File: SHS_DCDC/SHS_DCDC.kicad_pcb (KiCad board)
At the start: 4 copper layers, 100 x 100 mm, 104 parts, among them J1 Barrel_Jack, J2 USB_A, Q1 BSS84, Q10 PMV100XPEAR, Q11 PMV100XPEAR, Q12 PMV100XPEAR, Q13 PMV100XPEAR, Q2 PMV100XPEAR, Q3 2N7002, Q4 2N7002, Q5 PMV100XPEAR, Q6 2N7002, Q7 PMV100XPEAR, Q8 Q_PMOS_DGS, Q9 PMV100XPEAR, U1 A0Z1283, U2 INA181, U3 LMV324AIDR, U4 LMV358IDR, U5 MP3414A, U6 STM32G050K8T6, U7 MCP101

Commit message: 20213110
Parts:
- added U8: RT8299-WDFN10L, SHS_DCDC:RT8299-WDFN, F.Cu at (17.2, 67.2)
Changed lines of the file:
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@@
     (tracks 313)
     (zones 0)
-    (modules 104)
-    (nets 102)
+    (modules 105)
+    (nets 110)
   )
   (page A4)
@@
   )
   (setup
-    (last_trace_width 0.5)
+    (last_trace_width 0.25)
     (user_trace_width 0.4)
     (user_trace_width 0.5)
@@
   (net 100 MCU_TX)
   (net 101 "Net-(Q13-Pad1)")
+  (net 102 "Net-(U8-Pad1)")
+  (net 103 "Net-(U8-Pad2)")
+  (net 104 "Net-(U8-Pad3)")
+  (net 105 "Net-(U8-Pad4)")
+  (net 106 "Net-(U8-Pad7)")
+  (net 107 "Net-(U8-Pad6)")
+  (net 108 "Net-(U8-Pad8)")
+  (net 109 "Net-(U8-Pad10)")
   (net_class Default "This is the default net class."
     (clearance 0.2)
@@
     (add_net "Net-(U6-Pad8)")
     (add_net "Net-(U6-Pad9)")
+    (add_net "Net-(U8-Pad1)")
+    (add_net "Net-(U8-Pad10)")
+    (add_net "Net-(U8-Pad2)")
+    (add_net "Net-(U8-Pad3)")
+    (add_net "Net-(U8-Pad4)")
+    (add_net "Net-(U8-Pad6)")
+    (add_net "Net-(U8-Pad7)")
+    (add_net "Net-(U8-Pad8)")
     (add_net OP_CUR_BL1+)
     (add_net OP_CUR_BL1-)
@@
     (add_net V_MCU)
   )
+  (module SHS_DCDC:RT8299-WDFN (layer F.Cu)
+    (at 17.2 67.2)
+    (fp_text reference U8 (at 0.84 -2.337) (layer F.SilkS)
+      (effects (font (size 1 1) (thickness 0.15)))
+    )
+    (fp_text value RT8299-WDFN10L (at 10.365 2.337) (layer F.Fab)
+      (effects (font (size 1 1) (thickness 0.15)))
+    )
+    (fp_circle (center -2.636 -1.133) (end -2.486 -1.133) (layer F.SilkS) (width 0.2))
+    (fp_circle (center -2.636 -1.133) (end -2.486 -1.133) (layer F.Fab) (width 0.2))
+    (fp_line (start -1.53 -1.53) (end 1.53 -1.53) (layer F.Fab) (width 0.127))
+    (fp_line (start -1.53 1.53) (end 1.53 1.53) (layer F.Fab) (width 0.127))
+    (fp_line (start -1.53 -1.551) (end 1.53 -1.551) (layer F.SilkS) (width 0.127))
+    (fp_line (start -1.53 1.551) (end 1.53 1.551) (layer F.SilkS) (width 0.127))
+    (fp_line (start -1.53 -1.53) (end -1.53 1.53) (layer F.Fab) (width 0.127))
+    (fp_line (start 1.53 -1.53) (end 1.53 1.53) (layer F.Fab) (width 0.127))
+    (fp_line (start -2.1 -1.78) (end 2.1 -1.78) (layer F.CrtYd) (width 0.05))
+    (fp_line (start -2.1 1.78) (end 2.1 1.78) (layer F.CrtYd) (width 0.05))
+    (fp_line (start -2.1 -1.78) (end -2.1 1.78) (layer F.CrtYd) (width 0.05))
+    (fp_line (start 2.1 -1.78) (end 2.1 1.78) (layer F.CrtYd) (width 0.05))
+    (fp_poly (pts (xy -0.625 -1.045) (xy -0.095 -1.045) (xy -0.095 -0.095) (xy -0.625 -0.095)) (layer F.Paste) (width 0.01))
+    (fp_poly (pts (xy -0.625 0.095) (xy -0.095 0.095) (xy -0.095 1.045) (xy -0.625 1.045)) (layer F.Paste) (width 0.01))
+    (fp_poly (pts (xy 0.095 -1.045) (xy 0.625 -1.045) (xy 0.625 -0.095) (xy 0.095 -0.095)) (layer F.Paste) (width 0.01))
+    (fp_poly (pts (xy 0.095 0.095) (xy 0.625 0.095) (xy 0.625 1.045) (xy 0.095 1.045)) (layer F.Paste) (width 0.01))
+    (pad 1 smd roundrect (at -1.475 -1) (size 0.85 0.3) (layers F.Cu F.Paste F.Mask) (roundrect_rratio 0.03)
+      (net 102 "Net-(U8-Pad1)"))
+    (pad 2 smd roundrect (at -1.475 -0.5) (size 0.85 0.3) (layers F.Cu F.Paste F.Mask) (roundrect_rratio 0.03)
+      (net 103 "Net-(U8-Pad2)"))
+    (pad 3 smd roundrect (at -1.475 0) (size 0.85 0.3) (layers F.Cu F.Paste F.Mask) (roundrect_rratio 0.03)
+      (net 104 "Net-(U8-Pad3)"))
+    (pad 4 smd roundrect (at -1.475 0.5) (size 0.85 0.3) (layers F.Cu F.Paste F.Mask) (roundrect_rratio 0.03)
+      (net 105 "Net-(U8-Pad4)"))
+    (pad 5 smd roundrect (at -1.475 1) (size 0.85 0.3) (layers F.Cu F.Paste F.Mask) (roundrect_rratio 0.03))
+    (pad 6 smd roundrect (at 1.475 1) (size 0.85 0.3) (layers F.Cu F.Paste F.Mask) (roundrect_rratio 0.03)
+      (net 107 "Net-(U8-Pad6)"))
+    (pad 7 smd roundrect (at 1.475 0.5) (size 0.85 0.3) (layers F.Cu F.Paste F.Mask) (roundrect_rratio 0.03)
+      (net 106 "Net-(U8-Pad7)"))
+    (pad 8 smd roundrect (at 1.475 0) (size 0.85 0.3) (layers F.Cu F.Paste F.Mask) (roundrect_rratio 0.03)
+      (net 108 "Net-(U8-Pad8)"))
+    (pad 9 smd roundrect (at 1.475 -0.5) (size 0.85 0.3) (layers F.Cu F.Paste F.Mask) (roundrect_rratio 0.03))
+    (pad 10 smd roundrect (at 1.475 -1) (size 0.85 0.3) (layers F.Cu F.Paste F.Mask) (roundrect_rratio 0.03)
+      (net 109 "Net-(U8-Pad10)"))
+    (pad 11 smd rect (at 0 0) (size 1.7 2.55) (layers F.Cu F.Mask))
+  )
   (module Capacitor_SMD:C_0402_1005Metric (layer F.Cu)
     (at 76.4 70.5 270)
@@
     (fp_text value 100nF (at 0 1.16 90) (layer F.Fab)
       (effects (font (size 1 1) (thickness 0.15)))
-    )
-    (fp_text user %R (at 0 0 90) (layer F.Fab)
-      (effects (font (size 0.25 0.25) (thickness 0.04)))
     )
     (fp_line (start -0.5 0.25) (end -0.5 -0.25) (layer F.Fab) (width 0.1))
@@
     (fp_line (start 0.91 -0.46) (end 0.91 0.46) (layer F.CrtYd) (width 0.05))
     (fp_line (start 0.91 0.46) (end -0.91 0.46) (layer F.CrtYd) (width 0.05))
+    (fp_text user %R (at 0 0 90) (layer F.Fab)
+      (effects (font (size 0.25 0.25) (thickness 0.04)))
+    )
     (pad 2 smd roundrect (at 0.48 0 270) (size 0.56 0.62) (layers F.Cu F.Paste F.Mask) (roundrect_rratio 0.25)
       (net 15 V_MCU))
@@
     (fp_text value PMV100XPEAR (at 0.025 3.25) (layer F.Fab)
       (effects (font (size 1 1) (thickness 0.15)))
-    )
-    (fp_text user %R (at -0.125 0.15) (layer F.Fab)
-      (effects (font (size 0.25 0.25) (thickness 0.05)))
     )
     (fp_line (start -1.825 -1.95) (end 1.825 -1.95) (layer F.CrtYd) (width 0.05))
@@
     (fp_line (start -0.7 1.52) (end 0.7 1.52) (layer F.Fab) (width 0.1))
     (fp_line (start 0.7 1.52) (end 0.7 -1.52) (layer F.Fab) (width 0.1))
+    (fp_text user %R (at -0.125 0.15) (layer F.Fab)
+      (effects (font (size 0.25 0.25) (thickness 0.05)))
+    )
     (pad 1 smd rect (at -1.05 -0.95) (size 1.3 0.6) (layers F.Cu F.Paste F.Mask)
       (net 101 "Net-(Q13-Pad1)") (solder_mask_margin 0.07))
@@
     (fp_text value 4.7uF (at 0 1.43 90) (layer F.Fab)
       (effects (font (size 1 1) (thickness 0.15)))
-    )
-    (fp_text user %R (at 0 0 90) (layer F.Fab)
-      (effects (font (size 0.4 0.4) (thickness 0.06)))
     )
     (fp_line (start -0.8 0.4) (end -0.8 -0.4) (layer F.Fab) (width 0.1))
@@
     (fp_line (start 1.48 -0.73) (end 1.48 0.73) (layer F.CrtYd) (width 0.05))
     (fp_line (start 1.48 0.73) (end -1.48 0.73) (layer F.CrtYd) (width 0.05))
+    (fp_text user %R (at 0 0 90) (layer F.Fab)
+      (effects (font (size 0.4 0.4) (thickness 0.06)))
+    )
     (pad 2 smd roundrect (at 0.775 0 270) (size 0.9 0.95) (layers F.Cu F.Paste F.Mask) (roundrect_rratio 0.25)
       (net 15 V_MCU))
@@
     (fp_text value 10uF (at 0 1.43 90) (layer F.Fab)
       (effects (font (size 1 1) (thickness 0.15)))
-    )
-    (fp_text user %R (at 0 0 90) (layer F.Fab)
-      (effects (font (size 0.4 0.4) (thickness 0.06)))
     )
     (fp_line (start -0.8 0.4) (end -0.8 -0.4) (layer F.Fab) (width 0.1))
@@
     (fp_line (start 1.48 -0.73) (end 1.48 0.73) (layer F.CrtYd) (width 0.05))
     (fp_line (start 1.48 0.73) (end -1.48 0.73) (layer F.CrtYd) (width 0.05))
+    (fp_text user %R (at 0 0 90) (layer F.Fab)
+      (effects (font (size 0.4 0.4) (thickness 0.06)))
+    )
     (pad 2 smd roundrect (at 0.775 0 270) (size 0.9 0.95) (layers F.Cu F.Paste F.Mask) (roundrect_rratio 0.25)
       (net 13 DCDC_OUT))
@@
     (fp_text value 100nF (at 0 1.43) (layer F.Fab)
       (effects (font (size 1 1) (thickness 0.15)))
-    )
-    (fp_text user %R (at 0 0) (layer F.Fab)
-      (effects (font (size 0.4 0.4) (thickness 0.06)))
     )
     (fp_line (start -0.8 0.4) (end -0.8 -0.4) (layer F.Fab) (width 0.1))
@@
     (fp_line (start 1.48 -0.73) (end 1.48 0.73) (layer F.CrtYd) (width 0.05))
     (fp_line (start 1.48 0.73) (end -1.48 0.73) (layer F.CrtYd) (width 0.05))
+    (fp_text user %R (at 0 0) (layer F.Fab)
+      (effects (font (size 0.4 0.4) (thickness 0.06)))
+    )
     (pad 2 smd roundrect (at 0.775 0) (size 0.9 0.95) (layers F.Cu F.Paste F.Mask) (roundrect_rratio 0.25)
       (net 4 GND))

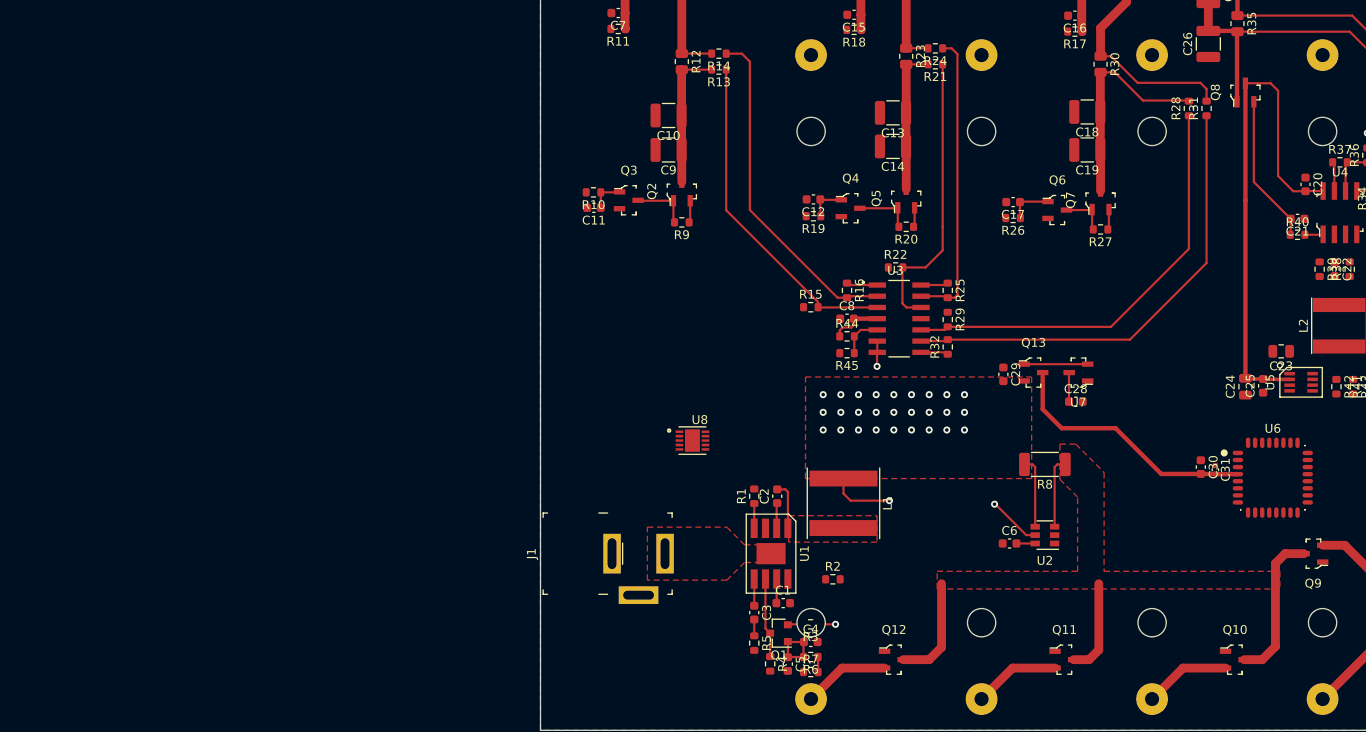
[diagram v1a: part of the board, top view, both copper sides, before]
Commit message: esp32 s2 mini placed
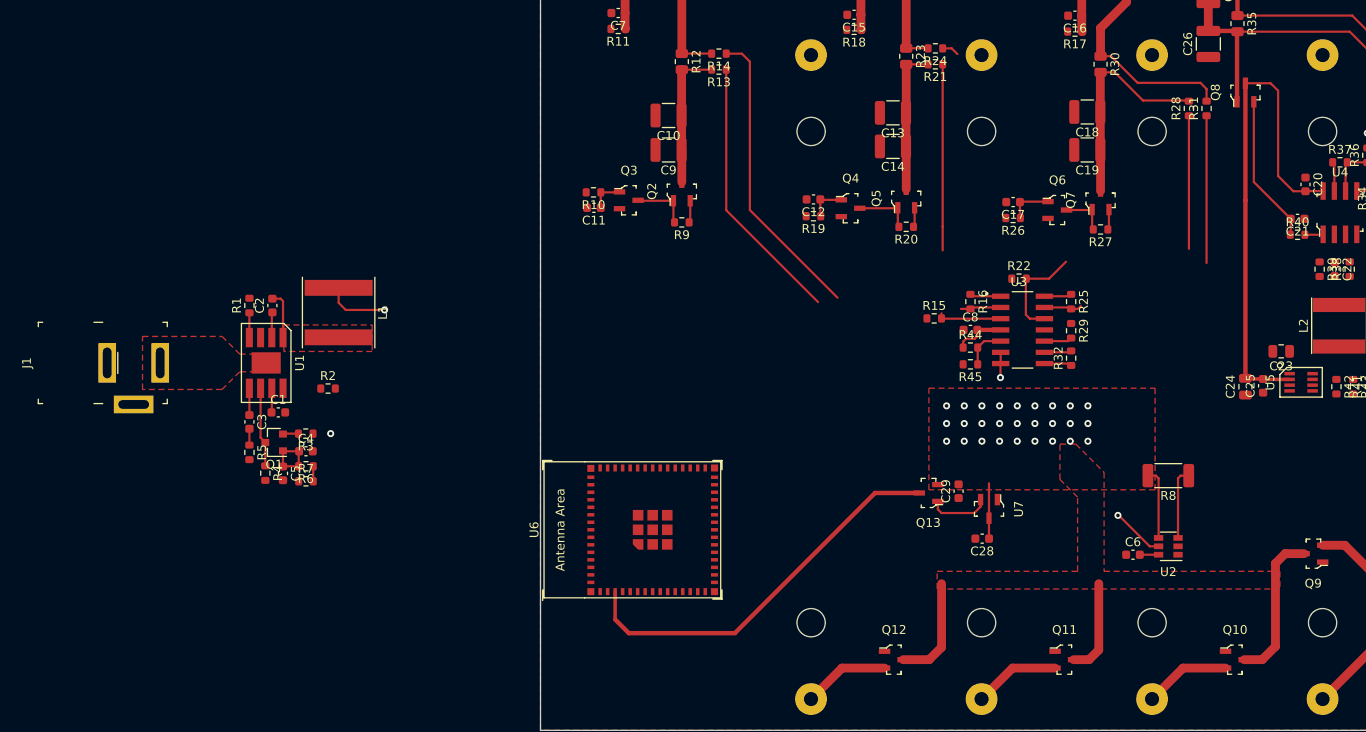
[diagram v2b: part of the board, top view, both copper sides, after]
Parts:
- removed C30: 4.7uF, Capacitor_SMD:C_0603_1608Metric
- removed C31: 100nF, Capacitor_SMD:C_0402_1005Metric
- removed U8: RT8299-WDFN10L, SHS_DCDC:RT8299-WDFN
- 4cells1: footprint SHS_DCDC:BK-18650-PC8 -> BK-18650:BK-18650-PC8
- U6: value STM32G050K8T6 -> ESP32-S2-MINI-1; footprint SHS_DCDC:STM320G50_LQFP32 -> Espressif:ESP32-S2-MINI-1
- moved U6 70.4 mm to (12.7, 77.3), turned to 90 degrees
- moved C2 61.1 mm to (-30.4, 51.9)
- moved C3 61.1 mm to (-33.0, 65.1)
- moved C4 61.1 mm to (-26.6, 68.4)
- moved R1 61.1 mm to (-33.0, 51.9)
- moved R2 61.1 mm to (-24.1, 61.3)
- moved R5 61.1 mm to (-33.0, 68.5)
- moved R6 61.1 mm to (-26.6, 70.1)
- moved R7 61.1 mm to (-26.6, 71.8)
- moved U1 61.1 mm to (-31.1, 58.4)
- moved C1 61.1 mm to (-29.7, 64.0)
- moved C5 61.1 mm to (-29.1, 70.9)
- moved J1 61.1 mm to (-46.0, 58.4)
- moved L1 61.1 mm to (-22.9, 52.7)
- moved Q1 61.1 mm to (-30.1, 67.4)
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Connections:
- Bulb1 pad 1: Net-(Bulb1-Pad1) -> (no net)
- Bulb2 pad 1: Net-(Bulb2-Pad1) -> (no net)
- R10 pad 2: MCU_PWM_TL -> (no net)
- R19 pad 2: MCU_PWM_BL1 -> (no net)
- R2 pad 2: Net-(R2-Pad2) -> (no net)
- R26 pad 2: MCU_PWM_BL2 -> (no net)
- R39 pad 2: ILIM_USB -> (no net)
- R41 pad 1: MCU_5V_EN -> (no net)
- TubeLight1 pad 2: Net-(TubeLight1-Pad2) -> (no net)
- U2 pad 1: MCU_ADC_BAT -> (no net)
- U6 pad 1: Net-(U6-Pad1) -> GND
- U6 pad 10: Net-(U6-Pad10) -> (no net)
- U6 pad 11: Net-(U6-Pad11) -> (no net)
- U6 pad 12: Net-(U6-Pad12) -> (no net)
- U6 pad 13: Net-(U6-Pad13) -> (no net)
- U6 pad 14: Net-(U6-Pad14) -> (no net)
- U6 pad 15: Net-(U6-Pad15) -> (no net)
- U6 pad 16: Net-(U6-Pad16) -> (no net)
- U6 pad 17: Net-(U6-Pad17) -> (no net)
- U6 pad 18: Net-(U6-Pad18) -> (no net)
- U6 pad 19: Net-(U6-Pad19) -> (no net)
- U6 pad 2: Net-(U6-Pad2) -> GND
- U6 pad 20: Net-(U6-Pad20) -> (no net)
- U6 pad 21: Net-(U6-Pad21) -> (no net)
- U6 pad 22: Net-(U6-Pad22) -> (no net)
- U6 pad 23: Net-(U6-Pad23) -> (no net)
- U6 pad 24: Net-(U6-Pad24) -> (no net)
- U6 pad 25: Net-(U6-Pad25) -> (no net)
- U6 pad 26: Net-(U6-Pad26) -> (no net)
- U6 pad 27: Net-(U6-Pad27) -> (no net)
- U6 pad 28: Net-(U6-Pad28) -> (no net)
- U6 pad 29: Net-(U6-Pad29) -> (no net)
- U6 pad 3: Net-(U6-Pad3) -> V_MCU
- U6 pad 30: MCU_TX -> GND
- U6 pad 31: MCU_RX -> (no net)
- U6 pad 32: Net-(U6-Pad32) -> (no net)
- U6 pad 4: V_MCU -> (no net)
- U6 pad 5: Net-(U6-Pad5) -> (no net)
- U6 pad 6: Net-(U6-Pad6) -> (no net)
- U6 pad 7: Net-(U6-Pad7) -> (no net)
- U6 pad 8: Net-(U6-Pad8) -> (no net)
- U6 pad 9: Net-(U6-Pad9) -> (no net)
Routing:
- net OP_CUR_BL2-: track 52.7 -> 19.8 mm
- net OP_CUR_BL2+: track 49.2 -> 18.2 mm
- net OP_CUR_BL1-: track 33.5 -> 6.27 mm
- net V_MCU: track 37.3 -> 52.8 mm
- net DCDC_OUT: track 45.3 -> 46.3 mm

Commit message: Commit_GitHubgDesktop
Try of Github desktop
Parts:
- removed C28: 100nF, Capacitor_SMD:C_0603_1608Metric
- removed R21, R24, R28, R31: 1k1%, Resistor_SMD:R_0603_1608Metric
- removed R22, R25, R29, R32: 20k1%, Resistor_SMD:R_0603_1608Metric
- removed R23, R30: 150mOhm, Resistor_SMD:R_0805_2012Metric
- removed R44, R45: 100k+, Resistor_SMD:R_0603_1608Metric
- added C30: 10 uF, Capacitor_SMD:C_0805_2012Metric, F.Cu at (22.0, 45.1)
- added C31: 10 uF, Capacitor_SMD:C_0805_2012Metric, F.Cu at (20.0, 45.1)
- added C32: 1 uF, Capacitor_SMD:C_0402_1005Metric, F.Cu at (28.5, 48.3)
- added C33: 10 uF, Capacitor_SMD:C_0603_1608Metric, F.Cu at (-17.2, 86.1)
- added C34: 10 uF, Capacitor_SMD:C_0603_1608Metric, F.Cu at (-21.2, 86.1)
- added Q14: 2N7002, Package_TO_SOT_SMD:SOT-23, F.Cu at (-25.4, 38.1)
- added Q15: MOSP_GENERIC, Package_TO_SOT_SMD:SOT-23, F.Cu at (88.9, -25.4)
- added Q16: MOSP_GENERIC, Package_TO_SOT_SMD:SOT-23, F.Cu at (84.0, -25.4)
- added Q17: MOSP_GENERIC, Package_TO_SOT_SMD:SOT-23, F.Cu at (127.2, -3.20)
- added R46: 1k, Resistor_SMD:R_0603_1608Metric, F.Cu at (-20.9, 39.6)
- added R47: 100k, Resistor_SMD:R_0402_1005Metric, F.Cu at (28.5, 49.4)
- added R48: 100k, Resistor_SMD:R_0603_1608Metric, F.Cu at (-21.2, 88.6)
- C1: value TBD -> 100nF; footprint Capacitor_SMD:C_0603_1608Metric -> Capacitor_SMD:C_0402_1005Metric
- C3: value 5.6nF -> 100nF
- C4, C5: value 10uF -> 22uF; footprint Capacitor_SMD:C_0603_1608Metric -> Capacitor_SMD:C_0805_2012Metric
- C8: footprint Capacitor_SMD:C_0603_1608Metric -> Capacitor_SMD:C_0402_1005Metric
- R1: value 100k -> R; footprint Resistor_SMD:R_0603_1608Metric -> Resistor_SMD:R_0402_1005Metric
- R12: value 150mOhm -> 100k 1%; footprint Resistor_SMD:R_0805_2012Metric -> Resistor_SMD:R_0402_1005Metric
- R13: value 1k1% -> 100k 1%; footprint Resistor_SMD:R_0603_1608Metric -> Resistor_SMD:R_0402_1005Metric
- R14: value 1k1% -> 100k+
- R15: value 20k1% -> 100k+
- R16: value 20k1% -> xxxmOhm; footprint Resistor_SMD:R_0603_1608Metric -> Resistor_SMD:R_1206_3216Metric
- R2: value R -> 1K 1%; footprint Resistor_SMD:R_0603_1608Metric -> Resistor_SMD:R_0402_1005Metric
- R5: value 10k -> 1K 1%; footprint Resistor_SMD:R_0603_1608Metric -> Resistor_SMD:R_0402_1005Metric
- U1: value A0Z1283 -> RT8299-WDFN10L; footprint SHS_DCDC:SOIC-8 -> Library:RT8299-WDFN
- U7: footprint digikey-footprints:SOT-23-3 -> Package_TO_SOT_SMD:SOT-23
- moved R5 176.3 mm to (117.9, -22.6), turned to 0 degrees
- moved R1 165.2 mm to (104.7, -39.4), turned to 0 degrees
- moved R2 162.4 mm to (115.0, -22.6)
- moved C3 160.3 mm to (121.6, 22.7), turned to 0 degrees
- moved U7 112.8 mm to (132.1, -3.20), turned to 0 degrees
- moved R12 110.4 mm to (115.0, -24.6), turned to 0 degrees
- moved R13 109.7 mm to (117.9, -24.6), turned to 0 degrees
- moved R14 101.4 mm to (121.6, 25.2), turned to 0 degrees
- moved C8 92.1 mm to (114.5, -9.80)
- moved R15 89.3 mm to (127.2, 19.4)
- moved R16 80.2 mm to (122.4, 19.8), turned to 0 degrees
- moved R4 69.3 mm to (35.1, 50.5), turned to 0 degrees
- moved U3 68.4 mm to (115.4, 23.3)
- moved R7 67.1 mm to (36.0, 47.6), turned to 90 degrees
- moved R6 64.9 mm to (34.3, 47.6), turned to -90 degrees
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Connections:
- Bulb1 pad 1: (no net) -> unconnected-(Bulb1-Pad1)
- Bulb2 pad 1: (no net) -> unconnected-(Bulb2-Pad1)
- C10 pad 1: Net-(C10-Pad1) -> LOAD_TL
- C13 pad 1: Net-(C13-Pad1) -> LOAD_BULB1
- C14 pad 1: Net-(C13-Pad1) -> LOAD_BULB1
- C18 pad 1: Net-(C18-Pad1) -> LOAD_BULB2
- C19 pad 1: Net-(C18-Pad1) -> LOAD_BULB2
- C23 pad 1: DCDC_OUT -> USB_IN
- C29 pad 2: DCDC_OUT -> V_MCU
- C3 pad 1: Net-(C3-Pad1) -> GND
- C3 pad 2: Net-(C3-Pad2) -> V_MCU
- C4 pad 1: Net-(C4-Pad1) -> DCDC_OUT
- C5 pad 1: Net-(C4-Pad1) -> DCDC_OUT
- C8 pad 1: GND -> VBAT
- C8 pad 2: V_MCU -> GND
- C9 pad 1: Net-(C10-Pad1) -> LOAD_TL
- J1 pad 1: Net-(J1-Pad1) -> Net-(C30-Pad1)
- L2 pad 2: DCDC_OUT -> USB_IN
- Q1 pad 1: Net-(C4-Pad1) -> Net-(C33-Pad1)
- Q13 pad 1: Net-(Q13-Pad1) -> unconnected-(Q13-Pad1)
- Q13 pad 2: DCDC_OUT -> LOAD
- Q2 pad 2: DCDC_OUT -> LOAD
- Q2 pad 3: Net-(C10-Pad1) -> LOAD_TL
- Q5 pad 2: DCDC_OUT -> LOAD
- Q5 pad 3: Net-(C13-Pad1) -> LOAD_BULB1
- Q7 pad 2: DCDC_OUT -> LOAD
- Q7 pad 3: Net-(C18-Pad1) -> LOAD_BULB2
- R1 pad 1: /FSW -> Net-(Q15-Pad3)
- R1 pad 2: GND -> MCU_PVBAT_DIRECT
- R10 pad 2: (no net) -> MCU_PWM_TL
- R12 pad 1: LOAD_TL -> OP_VS+
- R12 pad 2: Net-(C10-Pad1) -> GND
- R13 pad 1: OP_CUR_TL+ -> OP_VS-
- R13 pad 2: Net-(C10-Pad1) -> OP_VS
- R14 pad 1: OP_CUR_TL- -> V_MCU
- R14 pad 2: LOAD_TL -> Net-(R14-Pad2)
- R15 pad 1: GND -> Net-(R14-Pad2)
- R15 pad 2: OP_CUR_TL+ -> GND
- R16 pad 1: OP_FB_TL -> OP_V1+
- R16 pad 2: OP_CUR_TL- -> DCDC_OUT
- R19 pad 2: (no net) -> MCU_PWM_BL1
- R2 pad 1: /EN -> OP_V2-
- R2 pad 2: (no net) -> OP_VS+
- R20 pad 1: DCDC_OUT -> LOAD
- R26 pad 2: (no net) -> MCU_PWM_BL2
- R27 pad 1: DCDC_OUT -> LOAD
- R39 pad 2: (no net) -> ILIM_USB
- R41 pad 1: (no net) -> MCU_5V_EN
- R5 pad 1: Net-(C3-Pad2) -> OP_V1-
- R5 pad 2: GND -> OP_VS-
- R6 pad 2: Net-(C4-Pad1) -> Net-(C33-Pad1)
- R8 pad 1: VBAT -> Net-(R8-Pad1)
- R8 pad 2: DCDC_OUT -> LOAD
- R9 pad 1: DCDC_OUT -> LOAD
- TubeLight1 pad 2: (no net) -> unconnected-(TubeLight1-Pad2)
- U1 pad 2: Net-(C2-Pad1) -> Net-(Q1-Pad3)
- U1 pad 3: GND -> Net-(Q14-Pad3)
- U1 pad 4: /FSW -> Net-(C32-Pad1)
- U1 pad 6: Net-(Q1-Pad3) -> Net-(C30-Pad1)
- U1 pad 8: /EN -> Net-(C2-Pad1)
- U2 pad 1: (no net) -> MCU_ADC_BAT
- U2 pad 3: VBAT -> Net-(R8-Pad1)
- U2 pad 4: DCDC_OUT -> LOAD
- U3 pad 1: OP_FB_TL -> OP_V2-
- U3 pad 10: OP_CUR_BL2+ -> OP_V1+
- U3 pad 12: OP_CUR_BL1+ -> OP_VS+
- U3 pad 13: OP_CUR_BL1- -> OP_VS-
- U3 pad 14: OP_FB_BL1 -> OP_VS
- U3 pad 2: OP_CUR_TL- -> OP_V2-
- U3 pad 3: OP_CUR_TL+ -> DCDC_OUT
- U3 pad 5: Net-(R44-Pad2) -> Net-(R14-Pad2)
- U3 pad 8: OP_FB_BL2 -> OP_V1-
- U3 pad 9: OP_CUR_BL2- -> OP_V1-
- U5 pad 1: DCDC_OUT -> USB_IN
- U6 pad 10: (no net) -> unconnected-(U6-Pad10)
- U6 pad 11: (no net) -> unconnected-(U6-Pad11)
- U6 pad 12: (no net) -> unconnected-(U6-Pad12)
- U6 pad 13: (no net) -> unconnected-(U6-Pad13)
- U6 pad 14: (no net) -> unconnected-(U6-Pad14)
- U6 pad 15: (no net) -> unconnected-(U6-Pad15)
- U6 pad 16: (no net) -> unconnected-(U6-Pad16)
- U6 pad 17: (no net) -> unconnected-(U6-Pad17)
- U6 pad 18: (no net) -> unconnected-(U6-Pad18)
- U6 pad 19: (no net) -> unconnected-(U6-Pad19)
- U6 pad 20: (no net) -> unconnected-(U6-Pad20)
- U6 pad 21: (no net) -> unconnected-(U6-Pad21)
- U6 pad 22: (no net) -> unconnected-(U6-Pad22)
- U6 pad 23: (no net) -> unconnected-(U6-Pad23)
- U6 pad 24: (no net) -> unconnected-(U6-Pad24)
- U6 pad 25: (no net) -> unconnected-(U6-Pad25)
- U6 pad 26: (no net) -> unconnected-(U6-Pad26)
- U6 pad 27: (no net) -> unconnected-(U6-Pad27)
- U6 pad 28: (no net) -> unconnected-(U6-Pad28)
- U6 pad 29: (no net) -> unconnected-(U6-Pad29)
- U6 pad 31: (no net) -> unconnected-(U6-Pad31)
- U6 pad 32: (no net) -> unconnected-(U6-Pad32)
- U6 pad 33: (no net) -> unconnected-(U6-Pad33)
- U6 pad 34: (no net) -> unconnected-(U6-Pad34)
- U6 pad 35: (no net) -> unconnected-(U6-Pad35)
- U6 pad 36: (no net) -> unconnected-(U6-Pad36)
- U6 pad 37: (no net) -> unconnected-(U6-Pad37)
- U6 pad 38: (no net) -> unconnected-(U6-Pad38)
- U6 pad 39: (no net) -> unconnected-(U6-Pad39)
- U6 pad 4: (no net) -> unconnected-(U6-Pad4)
- U6 pad 40: (no net) -> unconnected-(U6-Pad40)
- U6 pad 41: (no net) -> unconnected-(U6-Pad41)
- U6 pad 44: (no net) -> unconnected-(U6-Pad44)
- U6 pad 45: (no net) -> unconnected-(U6-Pad45)
- U6 pad 5: (no net) -> unconnected-(U6-Pad5)
- U6 pad 6: (no net) -> unconnected-(U6-Pad6)
- U6 pad 7: (no net) -> unconnected-(U6-Pad7)
- U6 pad 8: (no net) -> unconnected-(U6-Pad8)
- U6 pad 9: (no net) -> unconnected-(U6-Pad9)
- U7 pad 2: Net-(Q13-Pad1) -> ODP_RESET
- U7 pad 3: DCDC_OUT -> VBAT
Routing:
- net OP_CUR_TL-: track 38.4 -> 0.00 mm
- net OP_CUR_TL+: track 37.9 -> 0.00 mm
- net DCDC_OUT: track 46.3 -> 10.0 mm, vias 29 -> 2
- net OP_CUR_BL1+: track 32.8 -> 0.00 mm
- net Net-(C18-Pad1): track 24.8 -> 0.00 mm
- net LOAD_BULB2: track 29.6 -> 54.3 mm
- net LOAD: track 0.00 -> 21.0 mm
- net OP_CUR_BL2-: track 19.8 -> 0.00 mm
- net OP_CUR_BL2+: track 18.2 -> 0.00 mm
- net Net-(C13-Pad1): track 16.6 -> 0.00 mm
- net LOAD_BULB1: track 15.0 -> 31.6 mm
- net Net-(C10-Pad1): track 16.1 -> 0.00 mm
- net V_MCU: track 52.8 -> 37.4 mm
- net VREF_BIDIRECTIONAL: track 34.0 -> 21.6 mm
- net Net-(R8-Pad1): track 0.00 -> 8.62 mm
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- added copper zone on F.Cu, net Net-(C30-Pad1)
- removed copper zone on F.Cu, net Net-(J1-Pad1)
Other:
- net class Default removed
